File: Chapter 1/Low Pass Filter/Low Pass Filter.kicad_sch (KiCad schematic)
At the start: 3 parts

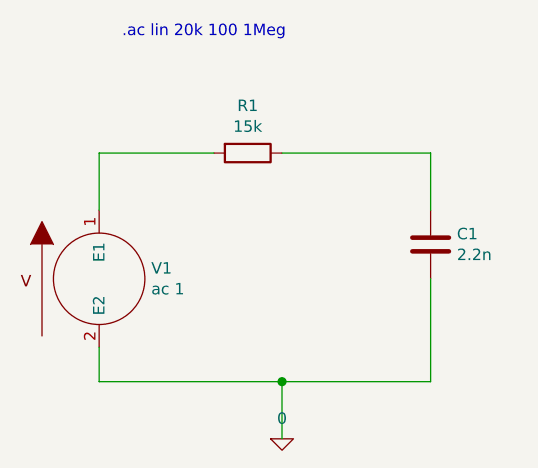
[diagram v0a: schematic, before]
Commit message: added v out tags to Chapter 1
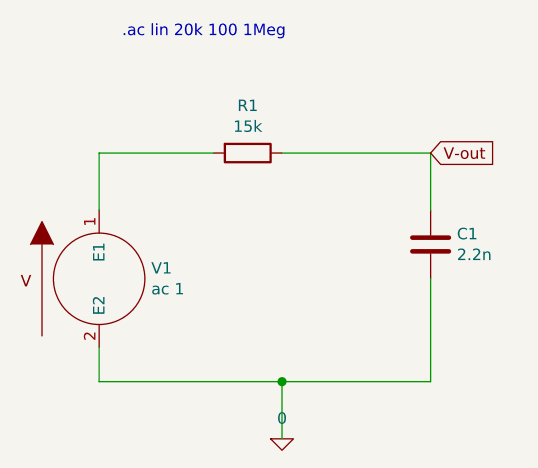
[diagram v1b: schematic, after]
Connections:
- net V-out: now reaches C1.2, R1.1
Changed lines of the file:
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@@
-(kicad_sch (version 20210406) (generator eeschema)
+(kicad_sch (version 20211123) (generator eeschema)
   (paper "A4")
-  (junction (at 88.9 63.5) (diameter 1.016) (color 0 0 0 0))
+  (junction (at 88.9 63.5) (diameter 1.016) (color 0 0 0 0)
+  )
+  (wire (pts (xy 88.9 69.85) (xy 88.9 63.5))
+    (stroke (width 0) (type solid) (color 0 0 0 0))
+  )
   (wire (pts (xy 68.58 38.1) (xy 81.28 38.1))
     (stroke (width 0) (type solid) (color 0 0 0 0))
   )
-  (wire (pts (xy 68.58 44.45) (xy 68.58 38.1))
+  (wire (pts (xy 88.9 63.5) (xy 105.41 63.5))
+    (stroke (width 0) (type solid) (color 0 0 0 0))
+  )
+  (wire (pts (xy 105.41 63.5) (xy 105.41 52.07))
+    (stroke (width 0) (type solid) (color 0 0 0 0))
+  )
+  (wire (pts (xy 105.41 38.1) (xy 105.41 44.45))
     (stroke (width 0) (type solid) (color 0 0 0 0))
   )
@@
     (stroke (width 0) (type solid) (color 0 0 0 0))
   )
-  (wire (pts (xy 88.9 38.1) (xy 105.41 38.1))
+  (wire (pts (xy 68.58 44.45) (xy 68.58 38.1))
     (stroke (width 0) (type solid) (color 0 0 0 0))
   )
-  (wire (pts (xy 88.9 63.5) (xy 105.41 63.5))
-    (stroke (width 0) (type solid) (color 0 0 0 0))
-  )
-  (wire (pts (xy 88.9 69.85) (xy 88.9 63.5))
-    (stroke (width 0) (type solid) (color 0 0 0 0))
-  )
-  (wire (pts (xy 105.41 38.1) (xy 105.41 44.45))
-    (stroke (width 0) (type solid) (color 0 0 0 0))
-  )
-  (wire (pts (xy 105.41 63.5) (xy 105.41 52.07))
+  (wire (pts (xy 88.9 38.1) (xy 105.41 38.1))
     (stroke (width 0) (type solid) (color 0 0 0 0))
   )
@@
     (effects (font (size 1.27 1.27)) (justify left bottom))
   )
-  (symbol (lib_id "Low-Pass-Filter-rescue:0-pspice") (at 88.9 69.85 0) (unit 1)
+  (global_label "V-out" (shape input) (at 105.41 38.1 0) (fields_autoplaced)
+    (effects (font (size 1.27 1.27)) (justify left))
+    (property "Intersheet References" "${INTERSHEET_REFS}" (id 0) (at 113.6984 38.0206 0)
+      (effects (font (size 1.27 1.27)) (justify left) hide)
+    )
+  )
+  (symbol (lib_id "Low-Pass-Filter-rescue:VSOURCE-pspice") (at 68.58 52.07 0) (unit 1)
     (in_bom yes) (on_board yes)
-    (property "Reference" "#GND01" (id 0) (at 88.9 72.39 0)
+    (property "Reference" "V1" (id 0) (at 74.3712 50.9016 0)
+      (effects (font (size 1.27 1.27)) (justify left))
+    )
+    (property "Value" "ac 1" (id 1) (at 74.3712 53.213 0)
+      (effects (font (size 1.27 1.27)) (justify left))
+    )
+    (property "Footprint" "" (id 2) (at 68.58 52.07 0)
       (effects (font (size 1.27 1.27)) hide)
     )
-    (property "Value" "0" (id 1) (at 88.9 67.5894 0))
-    (property "Footprint" "" (id 2) (at 88.9 69.85 0)
-      (effects (font (size 1.27 1.27)) hide)
-    )
-    (property "Datasheet" "~" (id 3) (at 88.9 69.85 0)
+    (property "Datasheet" "~" (id 3) (at 68.58 52.07 0)
       (effects (font (size 1.27 1.27)) hide)
     )
     (pin "1")
+    (pin "2")
   )
   (symbol (lib_id "Low-Pass-Filter-rescue:R-Device") (at 85.09 38.1 270) (unit 1)
@@
     (pin "2")
   )
-  (symbol (lib_id "Low-Pass-Filter-rescue:VSOURCE-pspice") (at 68.58 52.07 0) (unit 1)
+  (symbol (lib_id "Low-Pass-Filter-rescue:0-pspice") (at 88.9 69.85 0) (unit 1)
     (in_bom yes) (on_board yes)
-    (property "Reference" "V1" (id 0) (at 74.3712 50.9016 0)
-      (effects (font (size 1.27 1.27)) (justify left))
-    )
-    (property "Value" "ac 1" (id 1) (at 74.3712 53.213 0)
-      (effects (font (size 1.27 1.27)) (justify left))
-    )
-    (property "Footprint" "" (id 2) (at 68.58 52.07 0)
+    (property "Reference" "#GND01" (id 0) (at 88.9 72.39 0)
       (effects (font (size 1.27 1.27)) hide)
     )
-    (property "Datasheet" "~" (id 3) (at 68.58 52.07 0)
+    (property "Value" "0" (id 1) (at 88.9 67.5894 0))
+    (property "Footprint" "" (id 2) (at 88.9 69.85 0)
+      (effects (font (size 1.27 1.27)) hide)
+    )
+    (property "Datasheet" "~" (id 3) (at 88.9 69.85 0)
       (effects (font (size 1.27 1.27)) hide)
     )
     (pin "1")
-    (pin "2")
   )
   (sheet_instances
